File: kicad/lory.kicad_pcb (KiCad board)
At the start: 2 copper layers, 123.5 x 85.5 mm, 22 parts, among them J1 MJ-4PP-9, SW10 SW_PUSH, SW11 SW_PUSH, SW12 SW_PUSH, SW14 SW_PUSH, SW15 SW_PUSH, SW16 SW_PUSH, SW17 SW_PUSH, SW18 SW_PUSH, SW2 SW_PUSH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

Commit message: New alpha cluster
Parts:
- moved SW4 1.56 mm to (127.9, 50.1), turned to 2 degrees
- moved SW10 1.02 mm to (128.5, 67.1), turned to 2 degrees
- moved SW16 0.58 mm to (129.1, 84.1), turned to 2 degrees
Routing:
- net GND: track 505.2 -> 0.00 mm
- net SCL: track 119.2 -> 0.00 mm, vias 1 -> 0
- net row2: track 115.0 -> 0.00 mm, vias 1 -> 0
- net col4: track 110.4 -> 0.00 mm
- net col5: track 92.2 -> 0.00 mm
- net col1: track 89.8 -> 0.00 mm
- net row1: track 89.4 -> 0.00 mm, vias 1 -> 0
- net row3: track 82.9 -> 0.00 mm, vias 1 -> 0
- net col3: track 76.5 -> 0.00 mm
- net SDA: track 75.1 -> 0.00 mm, vias 1 -> 0
- net Net-(U1-Pad12): track 69.2 -> 0.00 mm, vias 1 -> 0
- net Net-(U1-Pad14): track 65.4 -> 0.00 mm
- net data: track 64.7 -> 0.00 mm
- net VCC: track 63.7 -> 0.00 mm
- net reset: track 58.3 -> 0.00 mm
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
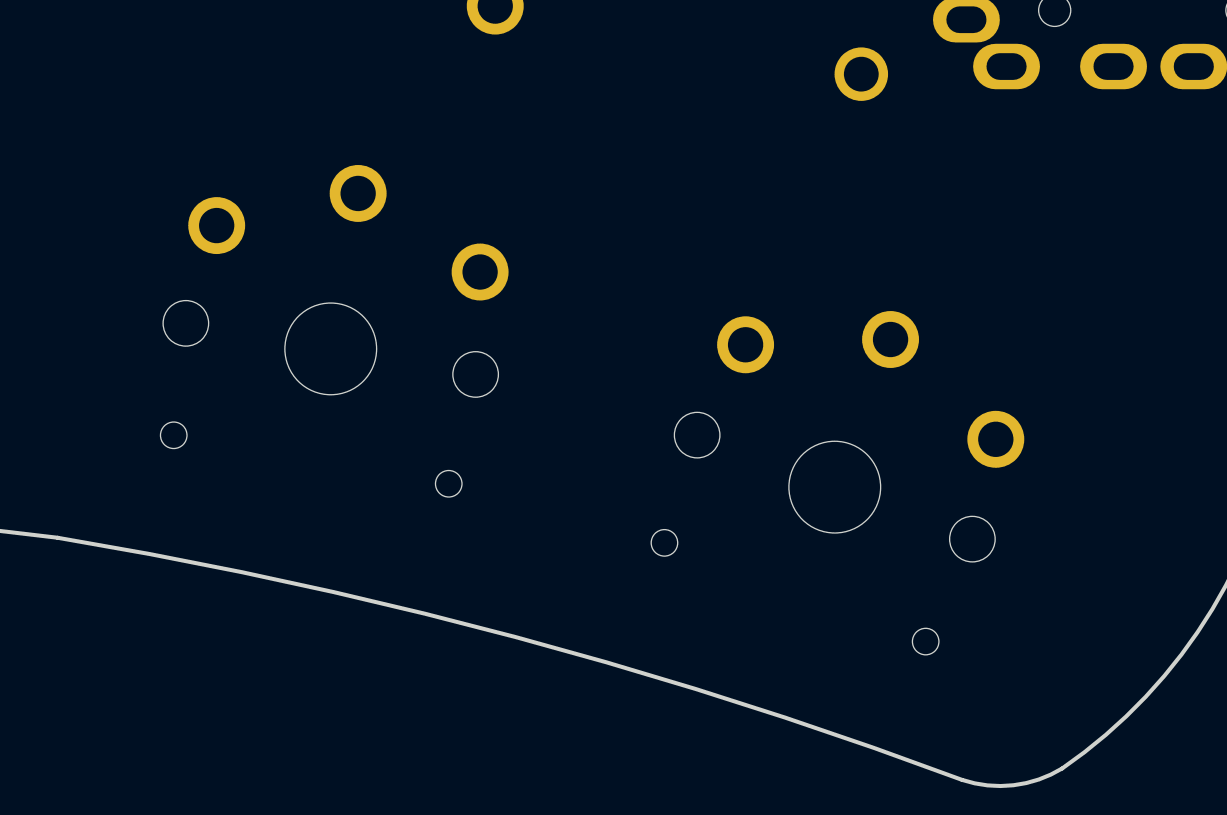
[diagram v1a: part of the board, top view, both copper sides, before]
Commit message: Update footprint lib
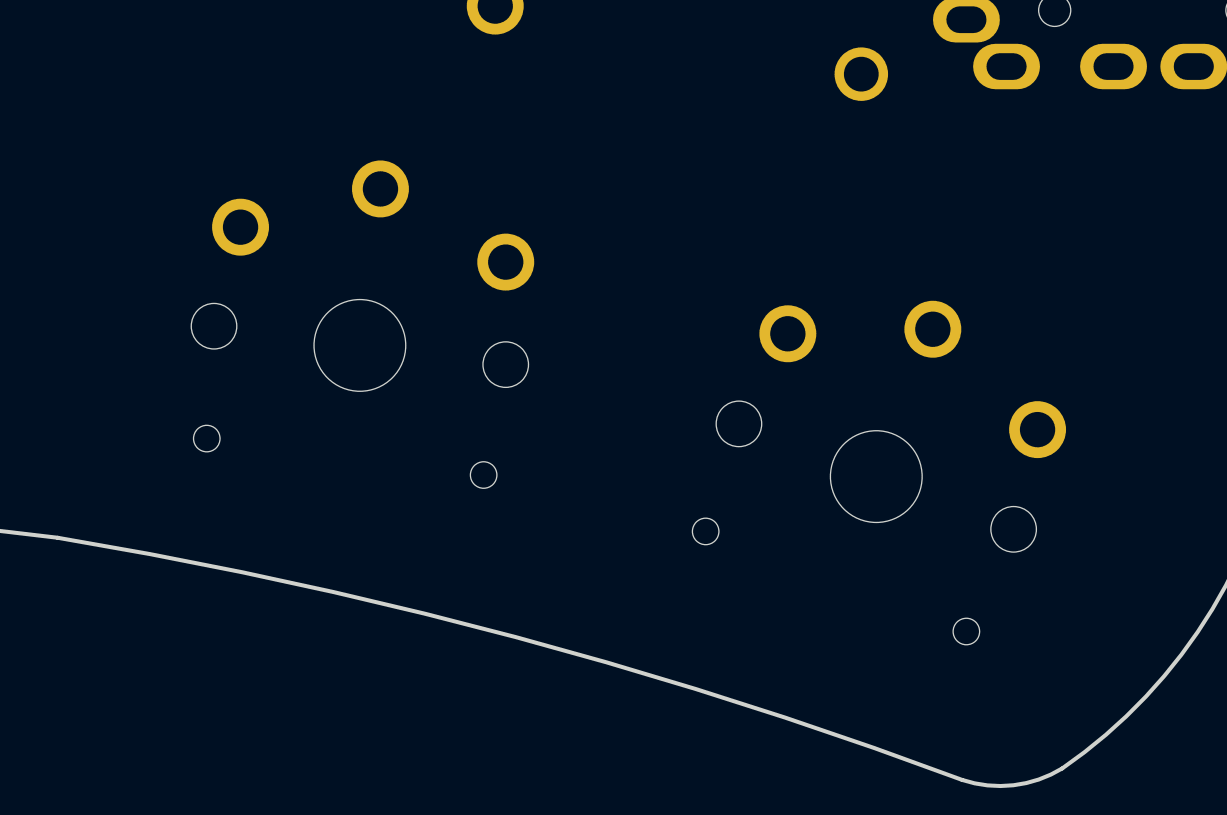
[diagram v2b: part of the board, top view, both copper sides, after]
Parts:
- moved SW21 1.60 mm to (179.7, 113.8), turned to 339 degrees
- moved SW20 1.10 mm to (160.3, 108.9), turned to 352.5 degrees
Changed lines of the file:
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@@
   )
   (module chocs:SW_PG1350_reversible_b2 (layer B.Cu)
-    (at 178.098 114.219 339.3)
+    (at 179.65 113.825 339)
     (descr "Kailh \"Choc\" PG1350 keyswitch, able to be mounted on front or back of PCB")
     (tags kailh,choc)
-    (fp_text reference SW21 (at 4.6 -6 159.3) (layer Dwgs.User) hide
+    (fp_text reference SW21 (at 4.6 -6 159) (layer Dwgs.User) hide
       (effects (font (size 1 1) (thickness 0.15)))
     )
-    (fp_text value SW_PUSH (at -0.5 -6 159.3) (layer Dwgs.User) hide
+    (fp_text value SW_PUSH (at -0.5 -6 159) (layer Dwgs.User) hide
       (effects (font (size 1 1) (thickness 0.15)))
     )
@@
     (fp_line (start 9 -8.5) (end 9 8.5) (layer Eco1.User) (width 0.12))
     (fp_line (start -9 -8.5) (end 9 -8.5) (layer Eco1.User) (width 0.12))
-    (fp_text user %R (at 0 0 339.3) (layer B.Fab)
+    (fp_text user %R (at 0 0 339) (layer B.Fab)
       (effects (font (size 1 1) (thickness 0.15)) (justify mirror))
     )
-    (fp_text user %R (at 0 0 339.3) (layer B.Fab)
+    (fp_text user %R (at 0 0 339) (layer B.Fab)
       (effects (font (size 1 1) (thickness 0.15)) (justify mirror))
     )
-    (fp_text user %V (at -0.000001 -8.255 339.3) (layer F.Fab)
+    (fp_text user %V (at -0.000001 -8.255 339) (layer F.Fab)
       (effects (font (size 1 1) (thickness 0.15)))
     )
-    (pad "" np_thru_hole circle (at -5.5 0 339.3) (size 1.7018 1.7018) (drill 1.7018) (layers *.Cu *.Mask))
-    (pad "" np_thru_hole circle (at 5.5 0 339.3) (size 1.7018 1.7018) (drill 1.7018) (layers *.Cu *.Mask))
-    (pad "" np_thru_hole circle (at 5.22 4.2 339.3) (size 0.9906 0.9906) (drill 0.9906) (layers *.Cu *.Mask))
-    (pad 1 thru_hole circle (at 0 -5.9 339.3) (size 2.128 2.128) (drill 1.32) (layers *.Cu *.Mask)
+    (pad "" np_thru_hole circle (at -5.5 0 339) (size 1.7018 1.7018) (drill 1.7018) (layers *.Cu *.Mask))
+    (pad "" np_thru_hole circle (at 5.5 0 339) (size 1.7018 1.7018) (drill 1.7018) (layers *.Cu *.Mask))
+    (pad "" np_thru_hole circle (at 5.22 4.2 339) (size 0.9906 0.9906) (drill 0.9906) (layers *.Cu *.Mask))
+    (pad 1 thru_hole circle (at 0 -5.9 339) (size 2.128 2.128) (drill 1.32) (layers *.Cu *.Mask)
       (net 20 "Net-(U1-Pad12)"))
-    (pad 2 thru_hole circle (at -5.000001 -3.8 339.3) (size 2.128 2.128) (drill 1.32) (layers *.Cu *.Mask)
+    (pad 2 thru_hole circle (at -5.000001 -3.8 339) (size 2.128 2.128) (drill 1.32) (layers *.Cu *.Mask)
       (net 6 GND))
-    (pad "" np_thru_hole circle (at 0 0 339.3) (size 3.429 3.429) (drill 3.429) (layers *.Cu *.Mask))
-    (pad 2 thru_hole circle (at 5 -3.8 339.3) (size 2.128 2.128) (drill 1.32) (layers *.Cu *.Mask)
+    (pad "" np_thru_hole circle (at 0 0 339) (size 3.429 3.429) (drill 3.429) (layers *.Cu *.Mask))
+    (pad 2 thru_hole circle (at 5 -3.8 339) (size 2.128 2.128) (drill 1.32) (layers *.Cu *.Mask)
       (net 6 GND))
-    (pad "" np_thru_hole circle (at -5.22 4.2 339.3) (size 0.9906 0.9906) (drill 0.9906) (layers *.Cu *.Mask))
+    (pad "" np_thru_hole circle (at -5.22 4.2 339) (size 0.9906 0.9906) (drill 0.9906) (layers *.Cu *.Mask))
   )
   (module chocs:SW_PG1350_reversible_b2 (layer B.Cu)
-    (at 159.255 109.051 350)
+    (at 160.344 108.921 352.5)
     (descr "Kailh \"Choc\" PG1350 keyswitch, able to be mounted on front or back of PCB")
     (tags kailh,choc)
-    (fp_text reference SW20 (at 4.600001 -6 350) (layer Dwgs.User) hide
+    (fp_text reference SW20 (at 4.600001 -6 352.5) (layer Dwgs.User) hide
       (effects (font (size 1 1) (thickness 0.15)))
     )
-    (fp_text value SW_PUSH (at -0.5 -5.999999 350) (layer Dwgs.User) hide
+    (fp_text value SW_PUSH (at -0.5 -5.999999 352.5) (layer Dwgs.User) hide
       (effects (font (size 1 1) (thickness 0.15)))
     )
@@
     (fp_line (start 9 -8.5) (end 9 8.5) (layer Eco1.User) (width 0.12))
     (fp_line (start -9 -8.5) (end 9 -8.5) (layer Eco1.User) (width 0.12))
-    (fp_text user %R (at 0 0 350) (layer B.Fab)
+    (fp_text user %R (at 0 0 352.5) (layer B.Fab)
       (effects (font (size 1 1) (thickness 0.15)) (justify mirror))
     )
-    (fp_text user %R (at 0 0 350) (layer B.Fab)
+    (fp_text user %R (at 0 0 352.5) (layer B.Fab)
       (effects (font (size 1 1) (thickness 0.15)) (justify mirror))
     )
-    (fp_text user %V (at 0 -8.255 350) (layer F.Fab)
+    (fp_text user %V (at 0 -8.255 352.5) (layer F.Fab)
       (effects (font (size 1 1) (thickness 0.15)))
     )
-    (fp_text user %R (at 0 0 350) (layer B.Fab)
+    (fp_text user %R (at 0 0 352.5) (layer B.Fab)
       (effects (font (size 1 1) (thickness 0.15)) (justify mirror))
     )
-    (pad "" np_thru_hole circle (at -5.5 0 350) (size 1.7018 1.7018) (drill 1.7018) (layers *.Cu *.Mask))
-    (pad "" np_thru_hole circle (at 5.5 0 350) (size 1.7018 1.7018) (drill 1.7018) (layers *.Cu *.Mask))
-    (pad "" np_thru_hole circle (at 5.22 4.2 350) (size 0.9906 0.9906) (drill 0.9906) (layers *.Cu *.Mask))
-    (pad 1 thru_hole circle (at 0 -5.9 350) (size 2.128 2.128) (drill 1.32) (layers *.Cu *.Mask)
+    (pad "" np_thru_hole circle (at -5.5 0 352.5) (size 1.7018 1.7018) (drill 1.7018) (layers *.Cu *.Mask))
+    (pad "" np_thru_hole circle (at 5.5 0 352.5) (size 1.7018 1.7018) (drill 1.7018) (layers *.Cu *.Mask))
+    (pad "" np_thru_hole circle (at 5.22 4.2 352.5) (size 0.9906 0.9906) (drill 0.9906) (layers *.Cu *.Mask))
+    (pad 1 thru_hole circle (at 0 -5.9 352.5) (size 2.128 2.128) (drill 1.32) (layers *.Cu *.Mask)
       (net 19 "Net-(U1-Pad13)"))
-    (pad 2 thru_hole circle (at -5 -3.8 350) (size 2.128 2.128) (drill 1.32) (layers *.Cu *.Mask)
+    (pad 2 thru_hole circle (at -5 -3.8 352.5) (size 2.128 2.128) (drill 1.32) (layers *.Cu *.Mask)
       (net 6 GND))
-    (pad "" np_thru_hole circle (at 0 0 350) (size 3.429 3.429) (drill 3.429) (layers *.Cu *.Mask))
-    (pad 2 thru_hole circle (at 5 -3.8 350) (size 2.128 2.128) (drill 1.32) (layers *.Cu *.Mask)
+    (pad "" np_thru_hole circle (at 0 0 352.5) (size 3.429 3.429) (drill 3.429) (layers *.Cu *.Mask))
+    (pad 2 thru_hole circle (at 5 -3.8 352.5) (size 2.128 2.128) (drill 1.32) (layers *.Cu *.Mask)
       (net 6 GND))
-    (pad "" np_thru_hole circle (at -5.22 4.2 350) (size 0.9906 0.9906) (drill 0.9906) (layers *.Cu *.Mask))
+    (pad "" np_thru_hole circle (at -5.22 4.2 352.5) (size 0.9906 0.9906) (drill 0.9906) (layers *.Cu *.Mask))
   )
   (module foostan:ResetSW (layer F.Cu)

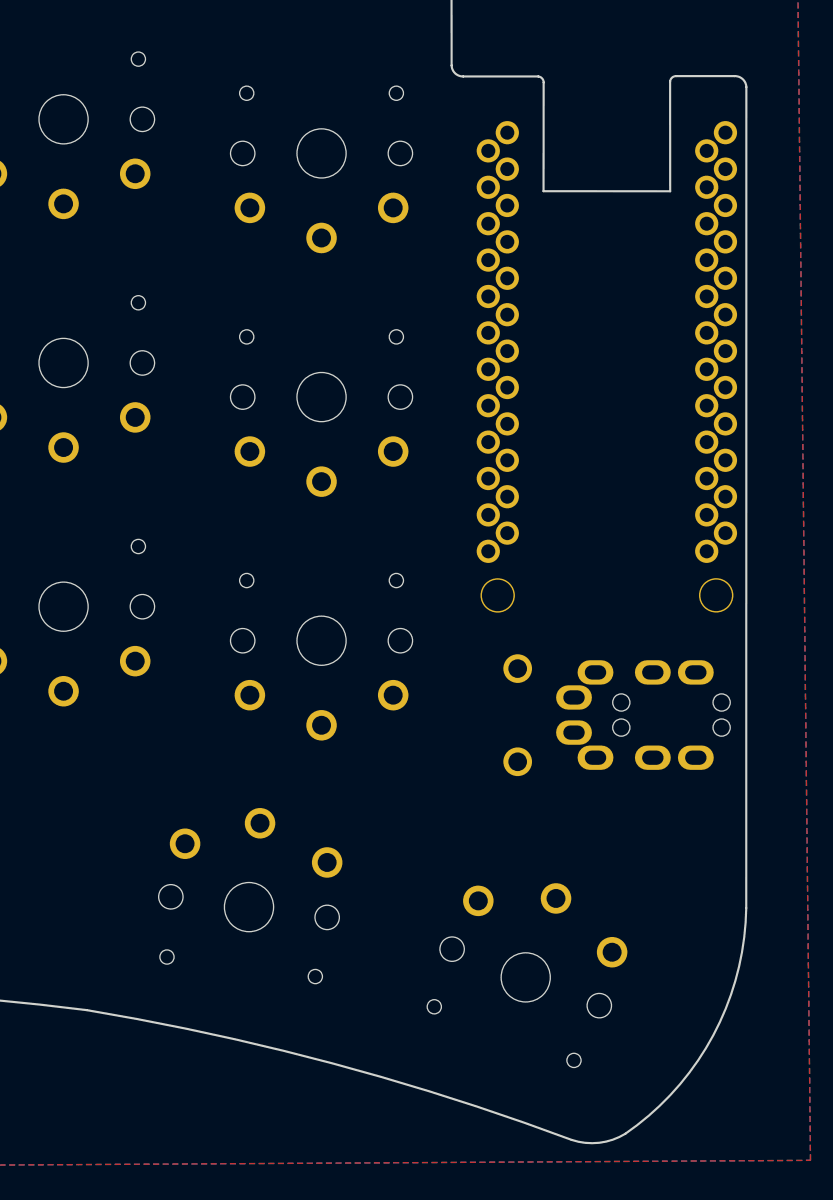
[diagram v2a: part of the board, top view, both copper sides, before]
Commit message: Thumbs further apart
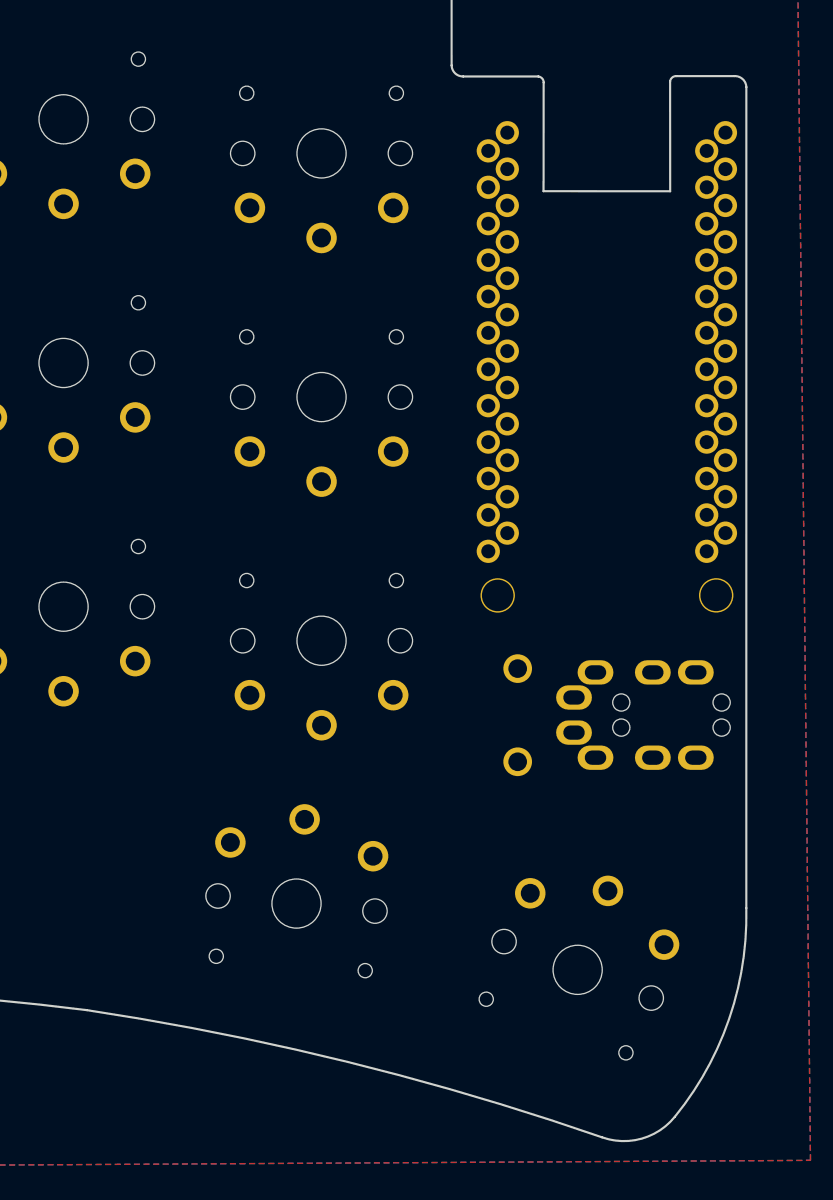
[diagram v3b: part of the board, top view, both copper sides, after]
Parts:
- moved SW21 3.66 mm to (183.3, 113.3)
- moved SW20 3.32 mm to (163.7, 108.7), turned to 354.5 degrees
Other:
- board size 123.5 x 85.5 mm -> 123.5 x 85.3 mm
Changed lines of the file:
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@@
     (pad_to_mask_clearance 0.2)
     (aux_axis_origin 168.195 30.895)
-    (grid_origin 181.444 87.237)
     (visible_elements FFFFE7FF)
     (pcbplotparams
@@
   )
   (module chocs:SW_PG1350_reversible_b2 (layer B.Cu)
-    (at 179.65 113.825 339)
+    (at 183.274 113.297 339)
     (descr "Kailh \"Choc\" PG1350 keyswitch, able to be mounted on front or back of PCB")
     (tags kailh,choc)
@@
   )
   (module chocs:SW_PG1350_reversible_b2 (layer B.Cu)
-    (at 160.344 108.921 352.5)
-    (descr "Kailh \"Choc\" PG1350 keyswitch, able to be mounted on front or back of PCB")
-    (tags kailh,choc)
-    (fp_text reference SW20 (at 4.600001 -6 352.5) (layer Dwgs.User) hide
-      (effects (font (size 1 1) (thickness 0.15)))
-    )
-    (fp_text value SW_PUSH (at -0.5 -5.999999 352.5) (layer Dwgs.User) hide
+    (at 163.658 108.673 354.5)
+    (descr "Kailh \"Choc\" PG1350 keyswitch, able to be mounted on front or back of PCB")
+    (tags kailh,choc)
+    (fp_text reference SW20 (at 4.600001 -6 354.5) (layer Dwgs.User) hide
+      (effects (font (size 1 1) (thickness 0.15)))
+    )
+    (fp_text value SW_PUSH (at -0.5 -5.999999 354.5) (layer Dwgs.User) hide
       (effects (font (size 1 1) (thickness 0.15)))
     )
@@
     (fp_line (start 9 -8.5) (end 9 8.5) (layer Eco1.User) (width 0.12))
     (fp_line (start -9 -8.5) (end 9 -8.5) (layer Eco1.User) (width 0.12))
-    (fp_text user %R (at 0 0 352.5) (layer B.Fab)
-      (effects (font (size 1 1) (thickness 0.15)) (justify mirror))
-    )
-    (fp_text user %R (at 0 0 352.5) (layer B.Fab)
-      (effects (font (size 1 1) (thickness 0.15)) (justify mirror))
-    )
-    (fp_text user %V (at 0 -8.255 352.5) (layer F.Fab)
-      (effects (font (size 1 1) (thickness 0.15)))
-    )
-    (fp_text user %R (at 0 0 352.5) (layer B.Fab)
-      (effects (font (size 1 1) (thickness 0.15)) (justify mirror))
-    )
-    (pad "" np_thru_hole circle (at -5.5 0 352.5) (size 1.7018 1.7018) (drill 1.7018) (layers *.Cu *.Mask))
-    (pad "" np_thru_hole circle (at 5.5 0 352.5) (size 1.7018 1.7018) (drill 1.7018) (layers *.Cu *.Mask))
-    (pad "" np_thru_hole circle (at 5.22 4.2 352.5) (size 0.9906 0.9906) (drill 0.9906) (layers *.Cu *.Mask))
-    (pad 1 thru_hole circle (at 0 -5.9 352.5) (size 2.128 2.128) (drill 1.32) (layers *.Cu *.Mask)
+    (fp_text user %R (at 0 0 354.5) (layer B.Fab)
+      (effects (font (size 1 1) (thickness 0.15)) (justify mirror))
+    )
+    (fp_text user %R (at 0 0 354.5) (layer B.Fab)
+      (effects (font (size 1 1) (thickness 0.15)) (justify mirror))
+    )
+    (fp_text user %V (at 0 -8.255 354.5) (layer F.Fab)
+      (effects (font (size 1 1) (thickness 0.15)))
+    )
+    (fp_text user %R (at 0 0 354.5) (layer B.Fab)
+      (effects (font (size 1 1) (thickness 0.15)) (justify mirror))
+    )
+    (pad "" np_thru_hole circle (at -5.5 0 354.5) (size 1.7018 1.7018) (drill 1.7018) (layers *.Cu *.Mask))
+    (pad "" np_thru_hole circle (at 5.5 0 354.5) (size 1.7018 1.7018) (drill 1.7018) (layers *.Cu *.Mask))
+    (pad "" np_thru_hole circle (at 5.22 4.2 354.5) (size 0.9906 0.9906) (drill 0.9906) (layers *.Cu *.Mask))
+    (pad 1 thru_hole circle (at 0 -5.9 354.5) (size 2.128 2.128) (drill 1.32) (layers *.Cu *.Mask)
       (net 19 "Net-(U1-Pad13)"))
-    (pad 2 thru_hole circle (at -5 -3.8 352.5) (size 2.128 2.128) (drill 1.32) (layers *.Cu *.Mask)
-      (net 6 GND))
-    (pad "" np_thru_hole circle (at 0 0 352.5) (size 3.429 3.429) (drill 3.429) (layers *.Cu *.Mask))
-    (pad 2 thru_hole circle (at 5 -3.8 352.5) (size 2.128 2.128) (drill 1.32) (layers *.Cu *.Mask)
-      (net 6 GND))
-    (pad "" np_thru_hole circle (at -5.22 4.2 352.5) (size 0.9906 0.9906) (drill 0.9906) (layers *.Cu *.Mask))
+    (pad 2 thru_hole circle (at -5 -3.8 354.5) (size 2.128 2.128) (drill 1.32) (layers *.Cu *.Mask)
+      (net 6 GND))
+    (pad "" np_thru_hole circle (at 0 0 354.5) (size 3.429 3.429) (drill 3.429) (layers *.Cu *.Mask))
+    (pad 2 thru_hole circle (at 5 -3.8 354.5) (size 2.128 2.128) (drill 1.32) (layers *.Cu *.Mask)
+      (net 6 GND))
+    (pad "" np_thru_hole circle (at -5.22 4.2 354.5) (size 0.9906 0.9906) (drill 0.9906) (layers *.Cu *.Mask))
   )
   (module foostan:ResetSW (layer F.Cu)
@@
       (net 15 reset))
   )
-  (gr_arc (start 119 296.015665) (end 149.044781 116.111726) (angle 11.0134138) (layer Edge.Cuts) (width 0.15))
+  (gr_arc (start 119 315) (end 149.044781 116.111726) (angle 10.5566717) (layer Edge.Cuts) (width 0.15))
   (gr_arc (start 190.14261 51.36) (end 190.14261 50.94) (angle -83.88406289) (layer Edge.Cuts) (width 0.15))
   (gr_line (start 180.895 58.97) (end 189.73 58.975) (layer Edge.Cuts) (width 0.15))
@@
   (gr_line (start 189.73 58.975) (end 189.725 51.315253) (layer Edge.Cuts) (width 0.15))
   (gr_line (start 180.895 58.97) (end 180.901441 51.382183) (layer Edge.Cuts) (width 0.15))
-  (gr_arc (start 184.27056 120.932523) (end 182.860064 125.164828) (angle -49.978482) (layer Edge.Cuts) (width 0.15))
+  (gr_arc (start 186.506496 120.688695) (end 184.974167 124.982518) (angle -70.66711935) (layer Edge.Cuts) (width 0.15))
   (gr_arc (start 90.27179 116.771466) (end 89.172412 117.201738) (angle -80.76911852) (layer Edge.Cuts) (width 0.15))
   (gr_arc (start 194.25 51.735) (end 195.045 51.71) (angle -90.72089035) (layer Edge.Cuts) (width 0.15))
   (gr_arc (start 175.275 50.17) (end 174.48 50.195) (angle -89.27976367) (layer Edge.Cuts) (width 0.15))
-  (gr_line (start 195.045 51.705) (end 195.037594 108.985022) (layer Edge.Cuts) (width 0.15))
+  (gr_line (start 195.045 51.705) (end 195.042003 108.990862) (layer Edge.Cuts) (width 0.15))
   (gr_line (start 175.29 50.965) (end 180.53 50.965) (layer Edge.Cuts) (width 0.15))
   (gr_line (start 174.48 50.195) (end 174.475405 44.009258) (layer Edge.Cuts) (width 0.15))
@@
   (gr_line (start 71.938953 64.242666) (end 89.172412 117.201738) (layer Edge.Cuts) (width 0.15))
   (gr_arc (start 125.5 301.492281) (end 90.520135 117.925628) (angle 18.02701016) (layer Edge.Cuts) (width 0.15))
-  (gr_arc (start 175.519578 108.66651) (end 186.604617 124.734376) (angle -54.46372486) (layer Edge.Cuts) (width 0.15))
+  (gr_arc (start 172.779743 109.5) (end 190.050908 123.556113) (angle -40.45049692) (layer Edge.Cuts) (width 0.15))
   (gr_arc (start 83.437551 61.245466) (end 78.610583 50.387227) (angle -80.64225145) (layer Edge.Cuts) (width 0.15))
   (gr_arc (start 139.2967 221.356359) (end 173.850849 43.257342) (angle -30.52241692) (layer Edge.Cuts) (width 0.15))
